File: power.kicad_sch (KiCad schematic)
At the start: 41 parts, among them U1 74HC86, U10 74AHC30, U11 74AHC30, U12 74AHC30, U13 74AHC30, U15 74LV32, U16 74AC109, U17 74LV32, U18 74LV04, U19 74LV08, U2 74HC00, U21 74AHC30, U22 74AHC30, U23 74AHC30, U24 74AHC30, U25 74AC109, U3 74LV27, U30 74LV08, U31 74LV08, U4 74HC00

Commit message: Make DRC quiet, add loooots of vias
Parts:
- U10, U11, U12, U13, U21, U22, U23, U24: symbol 74xx:74LS30 -> custom:74AHC30
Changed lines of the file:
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@@
     (stroke (width 0) (type default))
   )
-  (symbol (lib_id "74xx:74LS30") (at 121.92 116.84 0) (unit 2)
+  (symbol (lib_id "custom:74AHC30") (at 121.92 116.84 0) (unit 2)
     (in_bom yes) (on_board yes) (dnp no)
     (property "Reference" "U22" (at 118.11 115.57 0)
@@
     (pin "14")
     (pin "7")
+    (pin "10")
+    (pin "13")
+    (pin "9")
     (instances
       (project "6502gpu"
@@
     )
   )
-  (symbol (lib_id "74xx:74LS30") (at 53.34 43.18 0) (unit 2)
+  (symbol (lib_id "custom:74AHC30") (at 53.34 43.18 0) (unit 2)
     (in_bom yes) (on_board yes) (dnp no)
     (property "Reference" "U21" (at 49.53 41.91 0)
@@
     (pin "14")
     (pin "7")
+    (pin "10")
+    (pin "13")
+    (pin "9")
     (instances
       (project "6502gpu"
@@
     )
   )
-  (symbol (lib_id "74xx:74LS30") (at 193.04 43.18 0) (unit 2)
+  (symbol (lib_id "custom:74AHC30") (at 193.04 43.18 0) (unit 2)
     (in_bom yes) (on_board yes) (dnp no)
     (property "Reference" "U24" (at 189.23 41.91 0)
@@
     (pin "14")
     (pin "7")
+    (pin "10")
+    (pin "13")
+    (pin "9")
     (instances
       (project "6502gpu"
@@
     )
   )
-  (symbol (lib_id "74xx:74LS30") (at 99.06 43.18 0) (unit 2)
+  (symbol (lib_id "custom:74AHC30") (at 99.06 43.18 0) (unit 2)
     (in_bom yes) (on_board yes) (dnp no)
     (property "Reference" "U10" (at 95.25 41.91 0)
@@
     (pin "14")
     (pin "7")
+    (pin "10")
+    (pin "13")
+    (pin "9")
     (instances
       (project "6502gpu"
@@
     )
   )
-  (symbol (lib_id "74xx:74LS30") (at 76.2 116.84 0) (unit 2)
+  (symbol (lib_id "custom:74AHC30") (at 76.2 116.84 0) (unit 2)
     (in_bom yes) (on_board yes) (dnp no)
     (property "Reference" "U23" (at 72.39 115.57 0)
@@
     (pin "14")
     (pin "7")
+    (pin "10")
+    (pin "13")
+    (pin "9")
     (instances
       (project "6502gpu"
@@
     )
   )
-  (symbol (lib_id "74xx:74LS30") (at 146.05 43.18 0) (unit 2)
+  (symbol (lib_id "custom:74AHC30") (at 146.05 43.18 0) (unit 2)
     (in_bom yes) (on_board yes) (dnp no)
     (property "Reference" "U12" (at 142.24 41.91 0)
@@
     (pin "14")
     (pin "7")
+    (pin "10")
+    (pin "13")
+    (pin "9")
     (instances
       (project "6502gpu"
@@
     )
   )
-  (symbol (lib_id "74xx:74LS30") (at 53.34 116.84 0) (unit 2)
+  (symbol (lib_id "custom:74AHC30") (at 53.34 116.84 0) (unit 2)
     (in_bom yes) (on_board yes) (dnp no)
     (property "Reference" "U13" (at 49.53 115.57 0)
@@
     (pin "14")
     (pin "7")
+    (pin "10")
+    (pin "13")
+    (pin "9")
     (instances
       (project "6502gpu"
@@
     )
   )
-  (symbol (lib_id "74xx:74LS30") (at 121.92 43.18 0) (unit 2)
+  (symbol (lib_id "custom:74AHC30") (at 121.92 43.18 0) (unit 2)
     (in_bom yes) (on_board yes) (dnp no)
     (property "Reference" "U11" (at 118.11 41.91 0)
@@
     (pin "14")
     (pin "7")
-    (instances
-      (project "6502gpu"
+    (pin "10")
+    (pin "13")
+    (pin "9")
+    (instances
+      (project "6502gpu"

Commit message: rev2 mostly done now
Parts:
- added C35: 10u, Capacitor_SMD:C_1206_3216Metric_Pad1.33x1.80mm_HandSolder, symbol Device:C
- added J19, J20: Conn_01x04, Connector_PinHeader_2.54mm:PinHeader_1x04_P2.54mm_Vertical, symbol Connector_Generic:Conn_01x04
- added J21: Barrel_Jack_Switch, Connector_BarrelJack:BarrelJack_CUI_PJ-102AH_Horizontal, symbol Connector:Barrel_Jack_Switch
- added J22: Conn_01x02, Connector_PinHeader_2.54mm:PinHeader_1x02_P2.54mm_Vertical, symbol Connector_Generic:Conn_01x02
- added U34: L7805, Package_TO_SOT_THT:TO-220-3_Horizontal_TabDown, symbol Regulator_Linear:L7805
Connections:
- net +5V: now also C35.1, J19.1 (Pin_1), J19.2 (Pin_2), J19.3 (Pin_3), J19.4 (Pin_4), J22.1 (Pin_1)
- net GND: now also C35.2, J20.1 (Pin_1), J20.2 (Pin_2), J20.3 (Pin_3), J20.4 (Pin_4), J21.2, J21.3, U34.2 (GND)
- new net: J21.1, U34.1 (IN)
- new net: J22.2 (Pin_2), U34.3 (OUT)

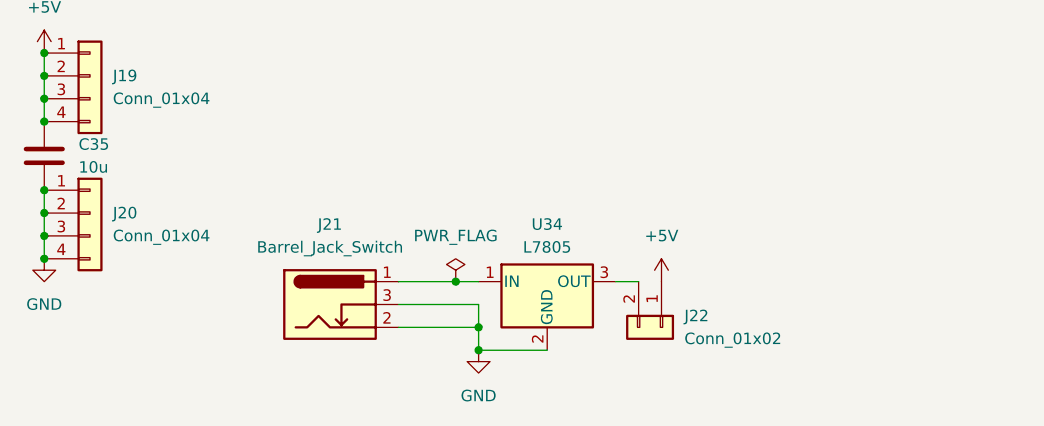
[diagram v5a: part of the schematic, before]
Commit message: add caps for 7805
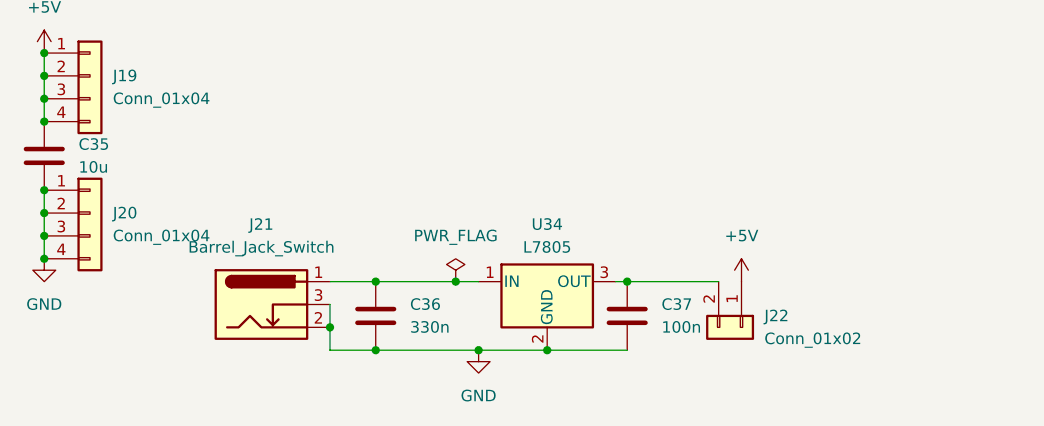
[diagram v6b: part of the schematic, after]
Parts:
- added C36: 330n, Capacitor_SMD:C_1206_3216Metric_Pad1.33x1.80mm_HandSolder, symbol Device:C
- added C37: 100n, Capacitor_SMD:C_1206_3216Metric_Pad1.33x1.80mm_HandSolder, symbol Device:C
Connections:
- net GND: now also C36.2, C37.2
- net at J21.1, U34.1 (IN): now also C36.1
- net at J22.2 (Pin_2), U34.3 (OUT): now also C37.1
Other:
- moved on the sheet: J21, J22
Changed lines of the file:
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@@
     (rev "2.0")
   )
+  (junction (at 107.95 182.88) (diameter 0) (color 0 0 0 0)
+  )
   (junction (at 121.92 67.31) (diameter 0) (color 0 0 0 0)
   )
@@
   (junction (at 130.81 30.48) (diameter 0) (color 0 0 0 0)
   )
+  (junction (at 107.95 175.26) (diameter 0) (color 0 0 0 0)
+  )
   (junction (at 53.34 67.31) (diameter 0) (color 0 0 0 0)
   )
@@
   (junction (at 71.12 165.1) (diameter 0) (color 0 0 0 0)
   )
+  (junction (at 127 182.88) (diameter 0) (color 0 0 0 0)
+  )
   (junction (at 170.18 104.14) (diameter 0) (color 0 0 0 0)
   )
@@
   (junction (at 201.93 55.88) (diameter 0) (color 0 0 0 0)
   )
-  (junction (at 119.38 180.34) (diameter 0) (color 0 0 0 0)
-  )
   (junction (at 179.07 92.71) (diameter 0) (color 0 0 0 0)
   )
@@
   (junction (at 146.05 92.71) (diameter 0) (color 0 0 0 0)
   )
+  (junction (at 135.89 175.26) (diameter 0) (color 0 0 0 0)
+  )
   (junction (at 121.92 104.14) (diameter 0) (color 0 0 0 0)
   )
@@
   (junction (at 154.94 55.88) (diameter 0) (color 0 0 0 0)
   )
+  (junction (at 102.87 180.34) (diameter 0) (color 0 0 0 0)
+  )
   (junction (at 62.23 129.54) (diameter 0) (color 0 0 0 0)
   )
@@
     (stroke (width 0) (type default))
   )
-  (wire (pts (xy 110.49 175.26) (xy 116.84 175.26))
+  (wire (pts (xy 102.87 175.26) (xy 107.95 175.26))
     (stroke (width 0) (type default))
   )
@@
     (stroke (width 0) (type default))
   )
-  (wire (pts (xy 119.38 180.34) (xy 119.38 182.88))
+  (wire (pts (xy 102.87 180.34) (xy 102.87 182.88))
     (stroke (width 0) (type default))
   )
@@
     (stroke (width 0) (type default))
   )
+  (wire (pts (xy 102.87 182.88) (xy 107.95 182.88))
+    (stroke (width 0) (type default))
+  )
   (wire (pts (xy 201.93 83.82) (xy 201.93 92.71))
     (stroke (width 0) (type default))
@@
     (stroke (width 0) (type default))
   )
+  (wire (pts (xy 127 182.88) (xy 135.89 182.88))
+    (stroke (width 0) (type default))
+  )
   (wire (pts (xy 193.04 30.48) (xy 201.93 30.48))
     (stroke (width 0) (type default))
@@
     (stroke (width 0) (type default))
   )
+  (wire (pts (xy 107.95 175.26) (xy 116.84 175.26))
+    (stroke (width 0) (type default))
+  )
   (wire (pts (xy 107.95 30.48) (xy 121.92 30.48))
     (stroke (width 0) (type default))
@@
     (stroke (width 0) (type default))
   )
+  (wire (pts (xy 135.89 175.26) (xy 146.05 175.26))
+    (stroke (width 0) (type default))
+  )
   (wire (pts (xy 179.07 67.31) (xy 179.07 76.2))
     (stroke (width 0) (type default))
   )
-  (wire (pts (xy 110.49 180.34) (xy 119.38 180.34))
-    (stroke (width 0) (type default))
-  )
   (wire (pts (xy 146.05 55.88) (xy 154.94 55.88))
     (stroke (width 0) (type default))
@@
     (stroke (width 0) (type default))
   )
-  (wire (pts (xy 134.62 175.26) (xy 137.16 175.26))
+  (wire (pts (xy 134.62 175.26) (xy 135.89 175.26))
     (stroke (width 0) (type default))
   )
@@
     (stroke (width 0) (type default))
   )
-  (wire (pts (xy 119.38 177.8) (xy 110.49 177.8))
-    (stroke (width 0) (type default))
-  )
   (wire (pts (xy 130.81 129.54) (xy 146.05 129.54))
     (stroke (width 0) (type default))
   )
+  (wire (pts (xy 107.95 182.88) (xy 119.38 182.88))
+    (stroke (width 0) (type default))
+  )
   (wire (pts (xy 107.95 30.48) (xy 107.95 39.37))
     (stroke (width 0) (type default))
@@
     (stroke (width 0) (type default))
   )
-  (wire (pts (xy 119.38 177.8) (xy 119.38 180.34))
+  (wire (pts (xy 102.87 177.8) (xy 102.87 180.34))
     (stroke (width 0) (type default))
   )
@@
         (path "/b1d8dca2-c863-4452-b293-53802be895cc/7de9712f-7078-4526-af23-f00b29ea7b26"
           (reference "U32") (unit 5)
+        )
+      )
+    )
+  )
+  (symbol (lib_id "Device:C") (at 135.89 179.07 0) (unit 1)
+    (in_bom yes) (on_board yes) (dnp no) (fields_autoplaced)
+    (property "Reference" "C37" (at 139.7 177.8 0)
+      (effects (font (size 1.27 1.27)) (justify left))
+    )
+    (property "Value" "100n" (at 139.7 180.34 0)
+      (effects (font (size 1.27 1.27)) (justify left))
+    )
+    (property "Footprint" "Capacitor_SMD:C_1206_3216Metric_Pad1.33x1.80mm_HandSolder" (at 136.8552 182.88 0)
+      (effects (font (size 1.27 1.27)) hide)
+    )
+    (property "Datasheet" "~" (at 135.89 179.07 0)
+      (effects (font (size 1.27 1.27)) hide)
+    )
+    (pin "1")
+    (pin "2")
+    (instances
+      (project "6502fb"
+        (path "/b1d8dca2-c863-4452-b293-53802be895cc/7de9712f-7078-4526-af23-f00b29ea7b26"
+          (reference "C37") (unit 1)
         )
       )
@@
     )
   )
-  (symbol (lib_id "Connector:Barrel_Jack_Switch") (at 102.87 177.8 0) (unit 1)
-    (in_bom yes) (on_board yes) (dnp no) (fields_autoplaced)
-    (property "Reference" "J21" (at 102.87 168.91 0)
+  (symbol (lib_id "Connector:Barrel_Jack_Switch") (at 95.25 177.8 0) (unit 1)
+    (in_bom yes) (on_board yes) (dnp no) (fields_autoplaced)
+    (property "Reference" "J21" (at 95.25 168.91 0)
       (effects (font (size 1.27 1.27)))
     )
-    (property "Value" "Barrel_Jack_Switch" (at 102.87 171.45 0)
+    (property "Value" "Barrel_Jack_Switch" (at 95.25 171.45 0)
       (effects (font (size 1.27 1.27)))
     )
-    (property "Footprint" "Connector_BarrelJack:BarrelJack_CUI_PJ-102AH_Horizontal" (at 104.14 178.816 0)
-      (effects (font (size 1.27 1.27)) hide)
-    )
-    (property "Datasheet" "~" (at 104.14 178.816 0)
+    (property "Footprint" "Connector_BarrelJack:BarrelJack_CUI_PJ-102AH_Horizontal" (at 96.52 178.816 0)
+      (effects (font (size 1.27 1.27)) hide)
+    )
+    (property "Datasheet" "~" (at 96.52 178.816 0)
       (effects (font (size 1.27 1.27)) hide)
     )
@@
     )
   )
-  (symbol (lib_id "power:+5V") (at 139.7 175.26 0) (unit 1)
-    (in_bom yes) (on_board yes) (dnp no) (fields_autoplaced)
-    (property "Reference" "#PWR02" (at 139.7 179.07 0)
-      (effects (font (size 1.27 1.27)) hide)
-    )
-    (property "Value" "+5V" (at 139.7 170.18 0)
+  (symbol (lib_id "power:+5V") (at 148.59 175.26 0) (unit 1)
+    (in_bom yes) (on_board yes) (dnp no) (fields_autoplaced)
+    (property "Reference" "#PWR02" (at 148.59 179.07 0)
+      (effects (font (size 1.27 1.27)) hide)
+    )
+    (property "Value" "+5V" (at 148.59 170.18 0)
       (effects (font (size 1.27 1.27)))
     )
-    (property "Footprint" "" (at 139.7 175.26 0)
-      (effects (font (size 1.27 1.27)) hide)
-    )
-    (property "Datasheet" "" (at 139.7 175.26 0)
+    (property "Footprint" "" (at 148.59 175.26 0)
+      (effects (font (size 1.27 1.27)) hide)
+    )
+    (property "Datasheet" "" (at 148.59 175.26 0)
       (effects (font (size 1.27 1.27)) hide)
     )
@@
     )
   )
+  (symbol (lib_id "Device:C") (at 107.95 179.07 0) (unit 1)
+    (in_bom yes) (on_board yes) (dnp no) (fields_autoplaced)
+    (property "Reference" "C36" (at 111.76 177.8 0)
+      (effects (font (size 1.27 1.27)) (justify left))
+    )
+    (property "Value" "330n" (at 111.76 180.34 0)
+      (effects (font (size 1.27 1.27)) (justify left))
+    )
+    (property "Footprint" "Capacitor_SMD:C_1206_3216Metric_Pad1.33x1.80mm_HandSolder" (at 108.9152 182.88 0)
+      (effects (font (size 1.27 1.27)) hide)
+    )
+    (property "Datasheet" "~" (at 107.95 179.07 0)
+      (effects (font (size 1.27 1.27)) hide)
+    )
+    (pin "1")
+    (pin "2")
+    (instances
+      (project "6502fb"
+        (path "/b1d8dca2-c863-4452-b293-53802be895cc/7de9712f-7078-4526-af23-f00b29ea7b26"
+          (reference "C36") (unit 1)
+        )
+      )
+    )
+  )
   (symbol (lib_id "74xx:74HC04") (at 76.2 43.18 0) (unit 7)
     (in_bom yes) (on_board yes) (dnp no)
@@
     )
   )
-  (symbol (lib_id "Connector_Generic:Conn_01x02") (at 139.7 180.34 270) (unit 1)
-    (in_bom yes) (on_board yes) (dnp no) (fields_autoplaced)
-    (property "Reference" "J22" (at 142.24 179.07 90)
-      (effects (font (size 1.27 1.27)) (justify left))
-    )
-    (property "Value" "Conn_01x02" (at 142.24 181.61 90)
-      (effects (font (size 1.27 1.27)) (justify left))
-    )
-    (property "Footprint" "Connector_PinHeader_2.54mm:PinHeader_1x02_P2.54mm_Vertical" (at 139.7 180.34 0)
-      (effects (font (size 1.27 1.27)) hide)
-    )
-    (property "Datasheet" "~" (at 139.7 180.34 0)
-      (effects (font (size 1.27 1.27)) hide)
-    )
+  (symbol (lib_id "Connector_Generic:Conn_01x02") (at 148.59 180.34 270) (unit 1)
+    (in_bom yes) (on_board yes) (dnp no) (fields_autoplaced)
+    (property "Reference" "J22" (at 151.13 179.07 90)
+      (effects (font (size 1.27 1.27)) (justify left))
+    )
+    (property "Value" "Conn_01x02" (at 151.13 181.61 90)
+      (effects (font (size 1.27 1.27)) (justify left))
+    )
+    (property "Footprint" "Connector_PinHeader_2.54mm:PinHeader_1x02_P2.54mm_Vertical" (at 148.59 180.34 0)
+      (effects (font (size 1.27 1.27)) hide)
+    )
+    (property "Datasheet" "~" (at 148.59 180.34 0)
+      (effects (font (size 1.27 1.27)) hide)
+    )
